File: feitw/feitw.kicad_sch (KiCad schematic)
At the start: 39 parts, among them J1 Out, J2 Eurorack_Power_10pin_Unshroud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, J3 Trig, Q1 BC847, Q2 BC847, Q3 BC847, U1 TLC555xD, U2 LM358

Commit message: feitw bugfixes
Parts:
- removed D3: LED, LED_THT:LED_D1.8mm_W3.3mm_H2.4mm, symbol Device:LED
- removed R9: 3k3, Resistor_THT:R_Axial_DIN0204_L3.6mm_D1.6mm_P1.90mm_Vertical, symbol Device:R
- added D2: LED, LED_THT:LED_D1.8mm_W3.3mm_H2.4mm, symbol Device:LED
- added Q4: BC847, Package_TO_SOT_SMD:SOT-23, symbol Transistor_BJT:BC847
- added R4: 3k3, Resistor_SMD:R_0805_2012Metric_Pad1.20x1.40mm_HandSolder, symbol Device:R
- C1, C4, C5, C7: footprint Capacitor_THT:C_Disc_D3.0mm_W1.6mm_P2.50mm -> Capacitor_SMD:C_0805_2012Metric_Pad1.18x1.45mm_HandSolder
- J2: footprint Connector_PinSocket_2.54mm:PinSocket_2x05_P2.54mm_Vertical -> mort_mix:PinHeader_2x05_P2.54mm_Vertical_shrouded
- R1, R10, R11, R12, R13, R14, R15, R2, R5, R6, R7, R8: footprint Resistor_THT:R_Axial_DIN0204_L3.6mm_D1.6mm_P1.90mm_Vertical -> Resistor_SMD:R_0805_2012Metric_Pad1.20x1.40mm_HandSolder
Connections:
- net +12V: now also D2.2 (A)
- net GND: now also Q4.2 (E)
- net at J1.T, R12.2: now also Q4.1 (B)
- new net: D2.1 (K), R4.1
- new net: Q4.3 (C), R4.2
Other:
- company: (none) -> Clandestine Circutry
- title: (none) -> Fastest Envelope in the West

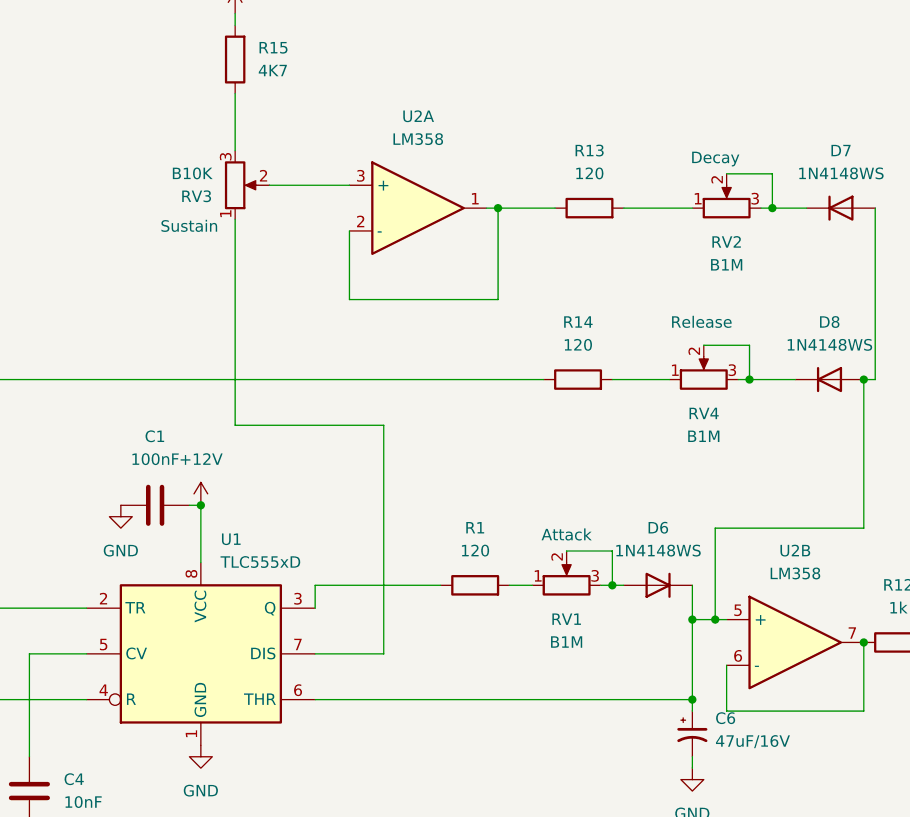
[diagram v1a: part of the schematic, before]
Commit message: created some boms
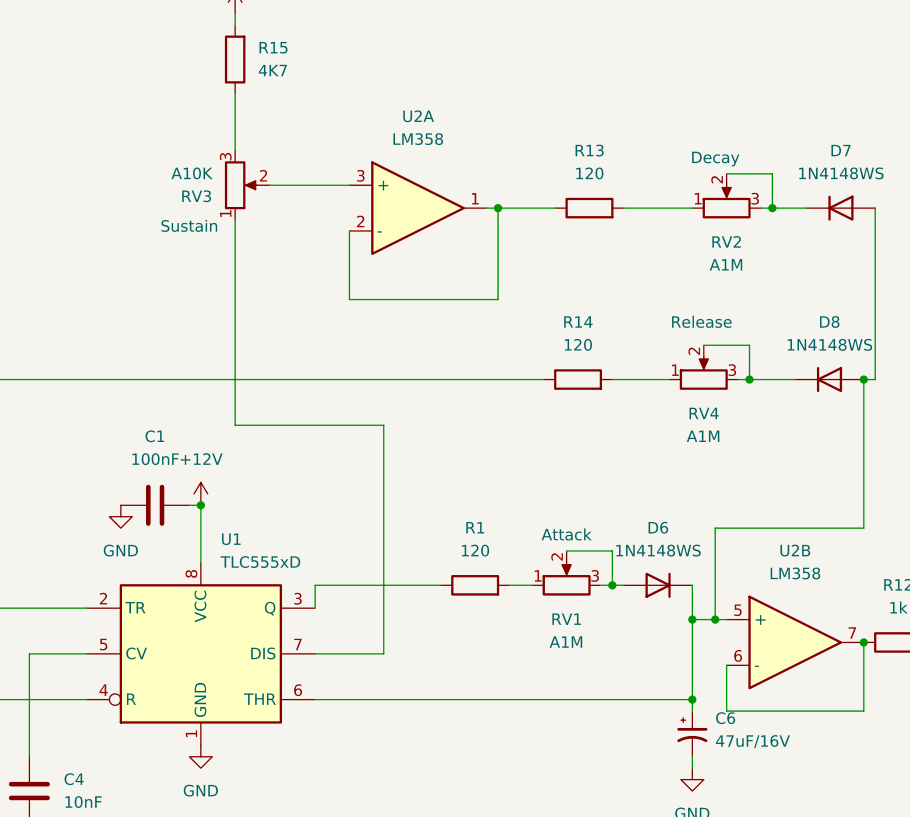
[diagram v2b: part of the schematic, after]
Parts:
- RV1, RV2, RV4: value B1M -> A1M
- RV3: value B10K -> A10K
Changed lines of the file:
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@@
 			)
 		)
-		(property "Value" "B1M"
+		(property "Value" "A1M"
 			(at 236.22 54.61 90)
 			(effects
@@
 			)
 		)
-		(property "Value" "B1M"
+		(property "Value" "A1M"
 			(at 233.68 73.66 90)
 			(effects
@@
 			)
 		)
-		(property "Value" "B10K"
+		(property "Value" "A10K"
 			(at 179.07 44.4501 0)
 			(effects
@@
 			)
 		)
-		(property "Value" "B1M"
+		(property "Value" "A1M"
 			(at 218.44 96.52 90)
 			(effects

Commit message: fixed some things
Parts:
- added R9: 47k, Resistor_SMD:R_0805_2012Metric_Pad1.20x1.40mm_HandSolder, symbol Device:R
- added RV5: 50k, symbol Device:R_Potentiometer_Trim
- added V1: VPWL, symbol Simulation_SPICE:VPWL
- added V2: 12, symbol Simulation_SPICE:VDC
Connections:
- net +12V: now also V2.1
- net GND: now also RV5.3, V1.2, V2.2
- net at R12.1, U2.6 (-), U2.7: now also R9.1
- net at J1.T, R12.2: no longer Q4.1 (B)
- new net: R9.2, RV5.1
- new net: Q4.1 (B), RV5.2
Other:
- moved on the sheet: D2
